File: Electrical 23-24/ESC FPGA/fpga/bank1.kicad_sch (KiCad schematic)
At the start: 1 part, among them U1 XC6SLX4-TQG144

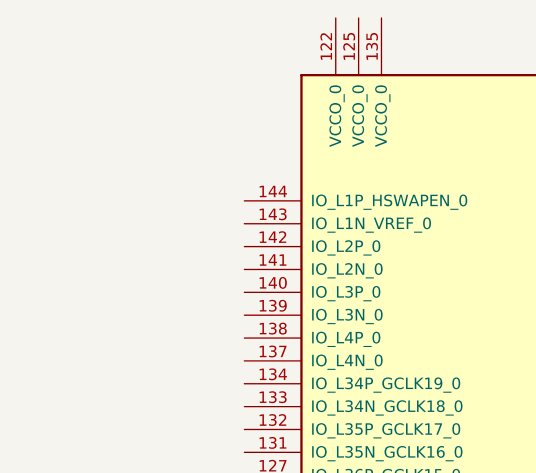
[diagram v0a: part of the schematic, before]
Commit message: Finish programming interface with FPGA
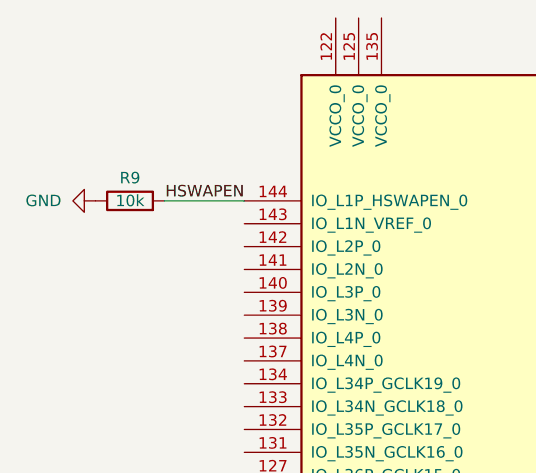
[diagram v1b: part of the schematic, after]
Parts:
- added R9: 10k, symbol Device:R
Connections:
- net HSWAPEN: now reaches U1.144 (IO_L1P_HSWAPEN_0)
- net HSWAPEN: now also R9.2
- new net GND: R9.1
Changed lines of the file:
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@@
 (kicad_sch (version 20230121) (generator eeschema)
   (paper "A4")
+  (wire (pts (xy 40.64 53.34) (xy 49.53 53.34))
+    (stroke (width 0) (type default))
+  )
+  (label "HSWAPEN" (at 49.53 53.34 180) (fields_autoplaced)
+    (effects (font (size 1.27 1.27)) (justify right bottom))
+  )
+  (symbol (lib_id "Device:R") (at 36.83 53.34 90) (unit 1)
+    (in_bom yes) (on_board yes) (dnp no)
+    (property "Reference" "R9" (at 36.83 50.8 90)
+      (effects (font (size 1.27 1.27)))
+    )
+    (property "Value" "10k" (at 36.83 53.34 90)
+      (effects (font (size 1.27 1.27)))
+    )
+    (property "Footprint" "" (at 36.83 55.118 90)
+      (effects (font (size 1.27 1.27)) hide)
+    )
+    (property "Datasheet" "~" (at 36.83 53.34 0)
+      (effects (font (size 1.27 1.27)) hide)
+    )
+    (pin "1")
+    (pin "2")
+    (instances
+      (project "fpga"
+        (path "/5bf59577-a814-4364-8f7a-37815cfb5474/1f83b38b-56ef-4110-879b-13379f9dd920"
+          (reference "R9") (unit 1)
+        )
+      )
+    )
+  )
+  (symbol (lib_id "power:GND") (at 33.02 53.34 270) (unit 1)
+    (in_bom yes) (on_board yes) (dnp no) (fields_autoplaced)
+    (property "Reference" "#PWR06" (at 26.67 53.34 0)
+      (effects (font (size 1.27 1.27)) hide)
+    )
+    (property "Value" "GND" (at 29.21 53.34 90)
+      (effects (font (size 1.27 1.27)) (justify right))
+    )
+    (property "Footprint" "" (at 33.02 53.34 0)
+      (effects (font (size 1.27 1.27)) hide)
+    )
+    (property "Datasheet" "" (at 33.02 53.34 0)
+      (effects (font (size 1.27 1.27)) hide)
+    )
+    (pin "1")
+    (instances
+      (project "fpga"
+        (path "/5bf59577-a814-4364-8f7a-37815cfb5474/a286b274-4434-47ab-983d-e64806fdcbd6"
+          (reference "#PWR06") (unit 1)
+        )
+        (path "/5bf59577-a814-4364-8f7a-37815cfb5474/1f83b38b-56ef-4110-879b-13379f9dd920"
+          (reference "#PWR07") (unit 1)
+        )
+      )
+    )
+  )
   (symbol (lib_id "FPGA_Xilinx_Spartan6:XC6SLX4-TQG144") (at 100.33 76.2 0) (unit 1)
     (in_bom yes) (on_board yes) (dnp no) (fields_autoplaced)

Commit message: idk but something
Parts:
- added C6 (x2): 4u7, symbol Device:C
- added C6 (x4): u47, symbol Device:C
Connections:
- net GND: now also C6.2, C6.2, C6.2, C6.2, C6.2, C6.2
- net VCCO_1: now reaches U1.103 (VCCO_1)
- net VCCO_1: now also U1.76 (VCCO_1), U1.86 (VCCO_1), C6.1, C6.1, C6.1
- net VCCO_0: now reaches U1.122 (VCCO_0)
- net VCCO_0: now also U1.125 (VCCO_0), U1.135 (VCCO_0), C6.1, C6.1, C6.1

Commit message: Add fpga stuff and stencils
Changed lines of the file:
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@@
+    )
+  )
+  (global_label "GND" (shape input) (at 270.51 27.94 90) (fields_autoplaced)
+    (effects (font (size 1.27 1.27)) (justify left))
+    (property "Intersheetrefs" "${INTERSHEET_REFS}" (at 270.51 21.0843 90)
+      (effects (font (size 1.27 1.27)) (justify left) hide)
     )
   )
@@
         )
       )
+    )
+  )
+  (symbol (lib_id "power:GND") (at 270.51 27.94 0) (unit 1)
+    (in_bom yes) (on_board yes) (dnp no) (fields_autoplaced)
+    (property "Reference" "#PWR016" (at 270.51 34.29 0)
+      (effects (font (size 1.27 1.27)) hide)
+    )
+    (property "Value" "GND" (at 270.51 33.02 0)
+      (effects (font (size 1.27 1.27)))
+    )
+    (property "Footprint" "" (at 270.51 27.94 0)
+      (effects (font (size 1.27 1.27)) hide)
+    )
+    (property "Datasheet" "" (at 270.51 27.94 0)
+      (effects (font (size 1.27 1.27)) hide)
+    )
+    (pin "1")
+    (instances
+      (project "fpga"
+        (path "/5bf59577-a814-4364-8f7a-37815cfb5474/3e04db34-3f8a-4742-be82-6fa24c009343"
+          (reference "#PWR016") (unit 1)
+        )
+        (path "/5bf59577-a814-4364-8f7a-37815cfb5474/1f83b38b-56ef-4110-879b-13379f9dd920"
+          (reference "#PWR037") (unit 1)
+        )
+        (path "/5bf59577-a814-4364-8f7a-37815cfb5474/a286b274-4434-47ab-983d-e64806fdcbd6"
+          (reference "#PWR036") (unit 1)
+        )
+      )

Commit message: Working on FPGA board
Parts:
- added J2: LSHM-110-04.0-L-DV-A-N-K-TR, LSHM-110-04.0-L-DV-A-N-K-TR:SAMTEC_LSHM-110-04.0-L-DV-A-N-K-TR, symbol fpga:LSHM-110-04.0-L-DV-A-N-K-TR
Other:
- note added: "where do I put the clock?"
- moved on the sheet: C6, R9, U1A

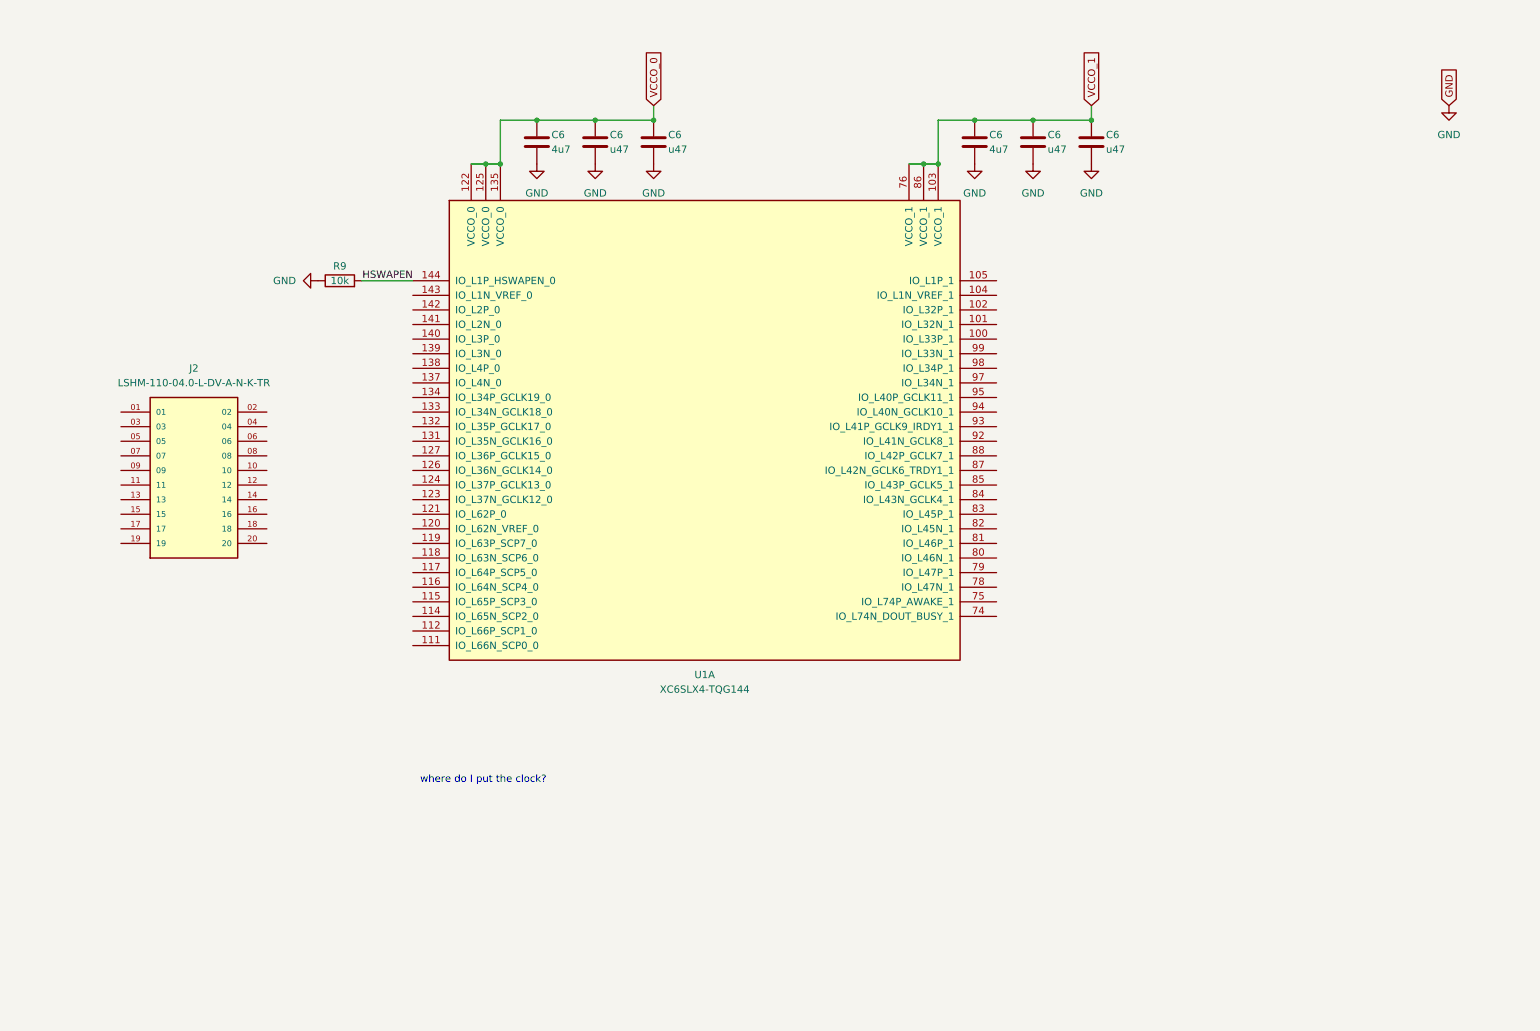
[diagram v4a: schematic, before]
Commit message: Add level shifters
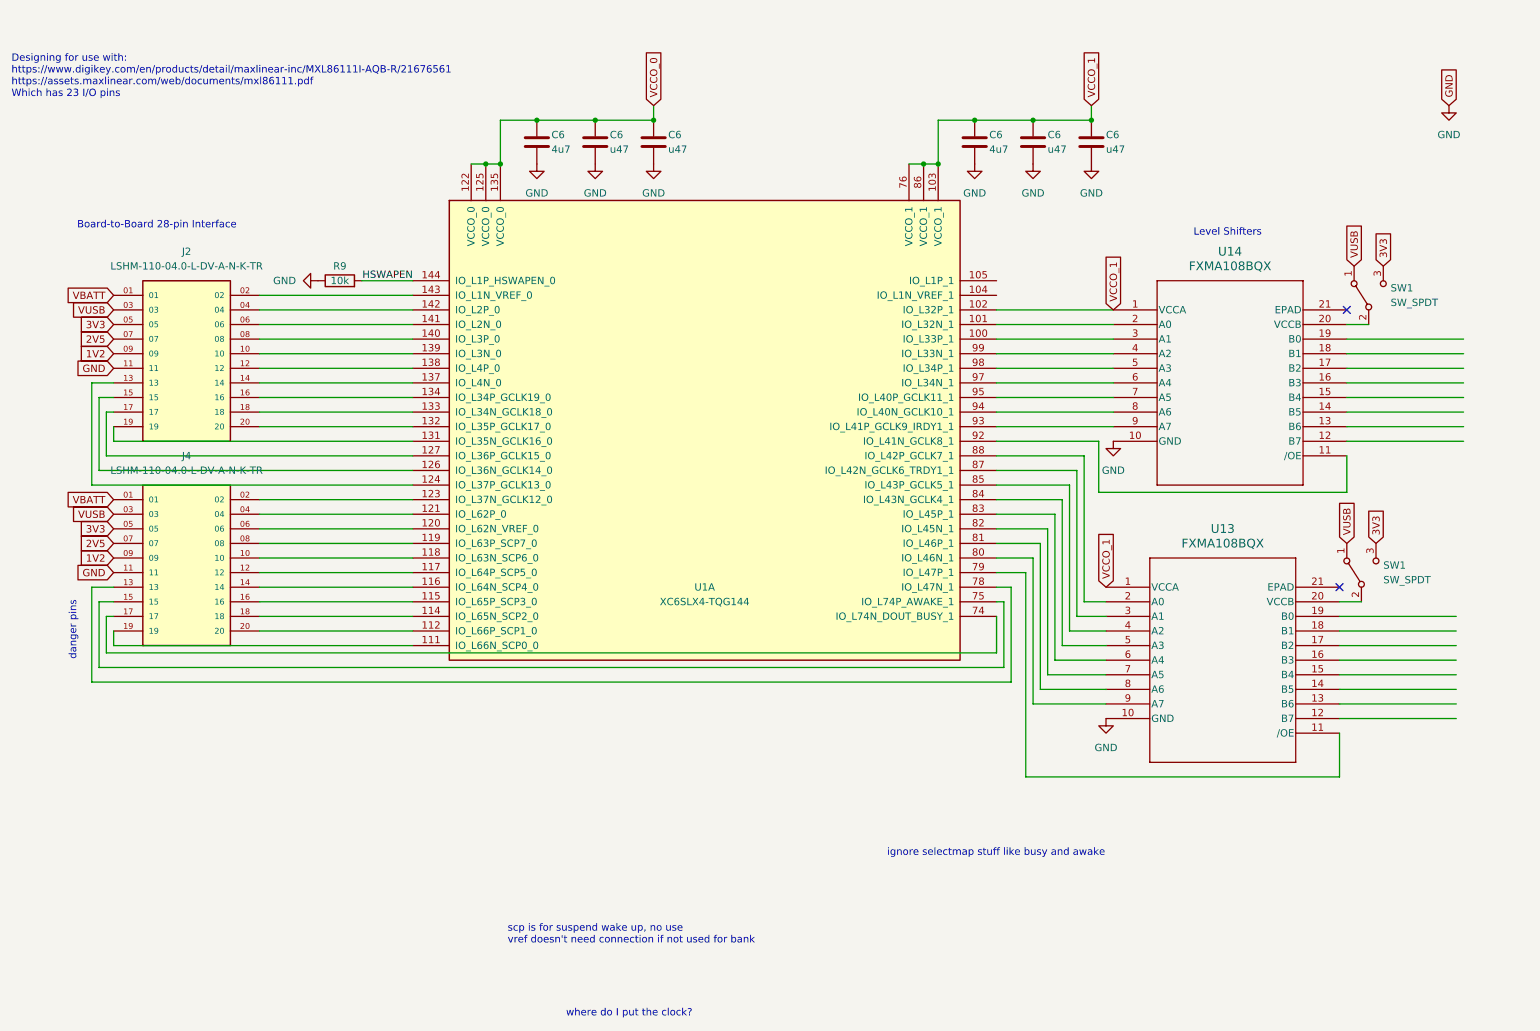
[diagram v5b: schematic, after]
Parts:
- added J4: LSHM-110-04.0-L-DV-A-N-K-TR, LSHM-110-04.0-L-DV-A-N-K-TR:SAMTEC_LSHM-110-04.0-L-DV-A-N-K-TR, symbol fpga:LSHM-110-04.0-L-DV-A-N-K-TR
- added SW1 (x2): SW_SPDT, symbol Switch:SW_SPDT
- added U13, U14: FXMA108BQX, WQFN20_2P5X4P5_ONS, symbol fpga:FXMA108BQX
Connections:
- net GND: now also J2.11, J4.11, U13.10 (GND), U14.10 (GND)
- net VCCO_1: now also U1.102 (IO_L32P_1), U13.1 (VCCA), U14.1 (VCCA)
- net VBATT: now reaches J2.01
- net VBATT: now also J4.01
- net at J2.02: now also U1.143 (IO_L1N_VREF_0)
- net VUSB: now reaches J2.03
- net VUSB: now also J4.03, SW1.1 (A), SW1.1 (A)
- net at J2.04: now also U1.142 (IO_L2P_0)
- net 3V3: now reaches J2.05
- net 3V3: now also J4.05, SW1.3 (C), SW1.3 (C)
- net at J2.06: now also U1.141 (IO_L2N_0)
- net 2V5: now reaches J2.07
- net 2V5: now also J4.07
- net at J2.08: now also U1.140 (IO_L3P_0)
- net 1V2: now reaches J2.09
- net 1V2: now also J4.09
- net at J2.10: now also U1.139 (IO_L3N_0)
- net at J2.12: now also U1.138 (IO_L4P_0)
- net at J2.13: now also U1.124 (IO_L37P_GCLK13_0)
- net at J2.14: now also U1.137 (IO_L4N_0)
- net at J2.15: now also U1.126 (IO_L36N_GCLK14_0)
- net at J2.16: now also U1.134 (IO_L34P_GCLK19_0)
- net at J2.17: now also U1.127 (IO_L36P_GCLK15_0)
- net at J2.18: now also U1.133 (IO_L34N_GCLK18_0)
- net at J2.19: now also U1.131 (IO_L35N_GCLK16_0)
- net at J2.20: now also U1.132 (IO_L35P_GCLK17_0)
- net at U1.100 (IO_L33P_1): now also U14.3 (A1)
- net at U1.101 (IO_L32N_1): now also U14.2 (A0)
- net at U1.111 (IO_L66N_SCP0_0): now also J4.19
- net at U1.112 (IO_L66P_SCP1_0): now also J4.20
- net at U1.114 (IO_L65N_SCP2_0): now also J4.18
- net at U1.115 (IO_L65P_SCP3_0): now also J4.16
- net at U1.116 (IO_L64N_SCP4_0): now also J4.14
- net at U1.117 (IO_L64P_SCP5_0): now also J4.12
- net at U1.118 (IO_L63N_SCP6_0): now also J4.10
- net at U1.119 (IO_L63P_SCP7_0): now also J4.08
- net at U1.120 (IO_L62N_VREF_0): now also J4.06
- net at U1.121 (IO_L62P_0): now also J4.04
- net at U1.123 (IO_L37N_GCLK12_0): now also J4.02
- net at U1.74 (IO_L74N_DOUT_BUSY_1): now also J4.17
- net at U1.75 (IO_L74P_AWAKE_1): now also J4.15
- net at U1.78 (IO_L47N_1): now also J4.13
- net at U1.79 (IO_L47P_1): now also U13.11 (/OE)
- net at U1.80 (IO_L46N_1): now also U13.9 (A7)
- net at U1.81 (IO_L46P_1): now also U13.8 (A6)
- net at U1.82 (IO_L45N_1): now also U13.7 (A5)
- net at U1.83 (IO_L45P_1): now also U13.6 (A4)
- net at U1.84 (IO_L43N_GCLK4_1): now also U13.5 (A3)
- net at U1.85 (IO_L43P_GCLK5_1): now also U13.4 (A2)
- net at U1.87 (IO_L42N_GCLK6_TRDY1_1): now also U13.3 (A1)
- net at U1.88 (IO_L42P_GCLK7_1): now also U13.2 (A0)
- net at U1.92 (IO_L41N_GCLK8_1): now also U14.11 (/OE)
- net at U1.93 (IO_L41P_GCLK9_IRDY1_1): now also U14.9 (A7)
- net at U1.94 (IO_L40N_GCLK10_1): now also U14.8 (A6)
- net at U1.95 (IO_L40P_GCLK11_1): now also U14.7 (A5)
- net at U1.97 (IO_L34N_1): now also U14.6 (A4)
- net at U1.98 (IO_L34P_1): now also U14.5 (A3)
- net at U1.99 (IO_L33N_1): now also U14.4 (A2)
- new net: SW1.2 (B), U13.20 (VCCB)
- new net: SW1.2 (B), U14.20 (VCCB)
- no-connect marks 0 -> 2
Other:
- note added: "Board-to-Board 28-pin Interface"
- note added: "Designing for use with: https://www.digikey.com/en/products/detail/maxlinear-inc/MXL86111I-AQB-R/21676561 https://assets.maxlinear.com/web/documents/mxl86111.pdf Which has 23 I/O pins"
- note added: "Level Shifters"
- note added: "danger pins"
- note added: "ignore selectmap stuff like busy and awake"
- note added: "scp is for suspend wake up, no use vref doesn't need connection if not used for bank"
- moved on the sheet: J2

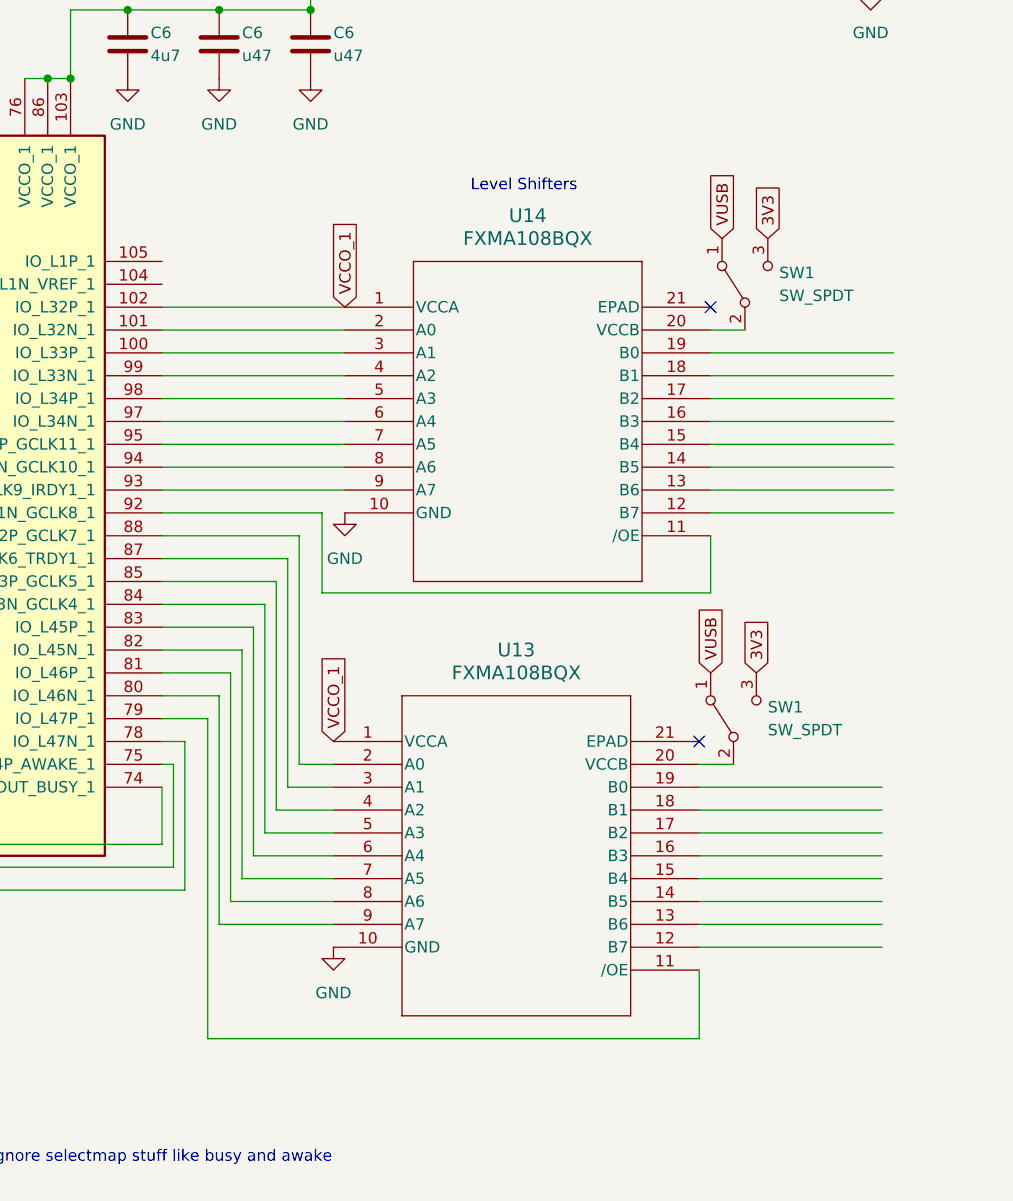
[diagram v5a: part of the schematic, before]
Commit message: Finished FPGA board schematic
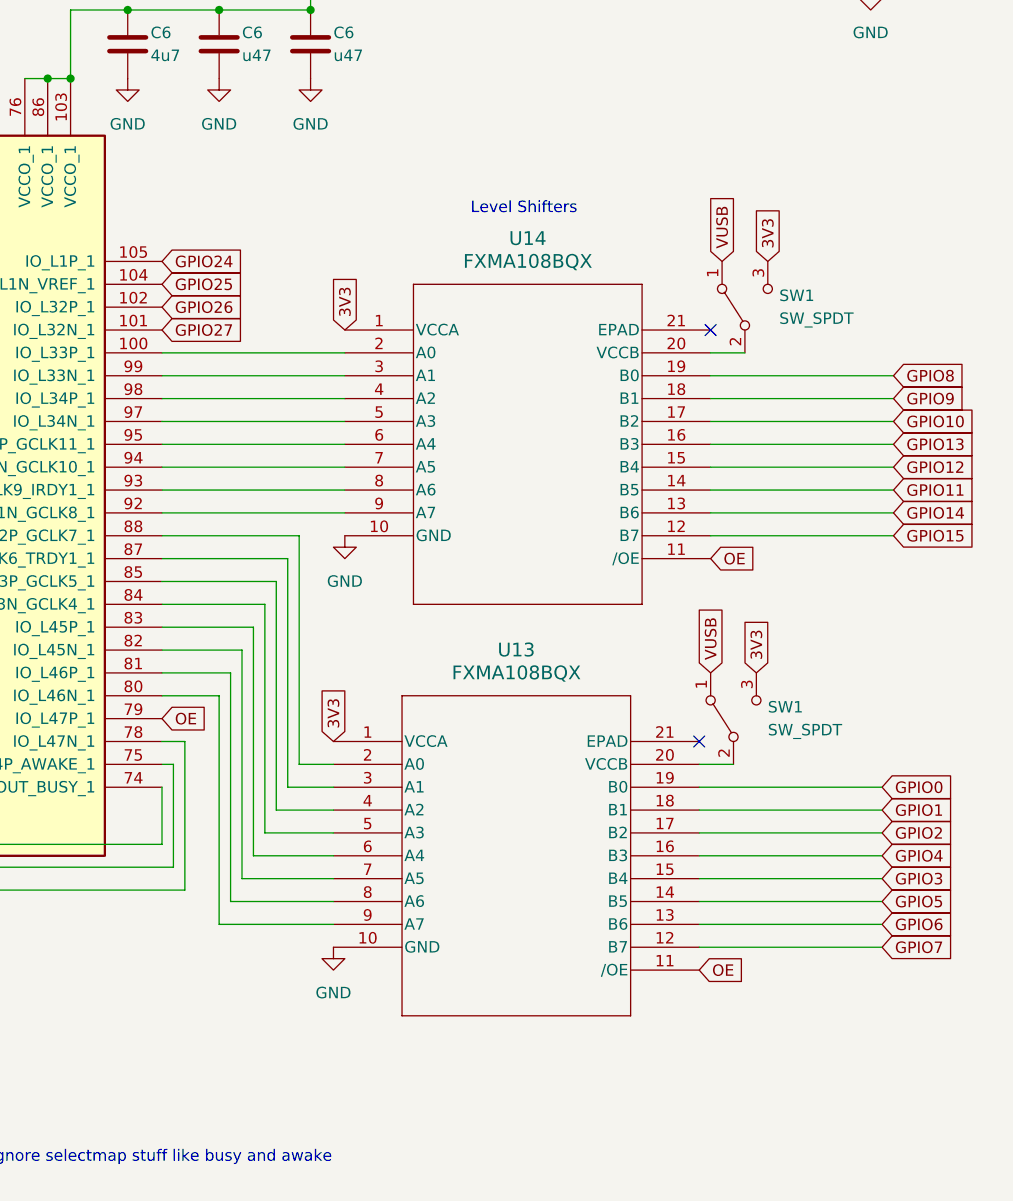
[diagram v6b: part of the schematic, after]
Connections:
- net 3V3: now also U13.1 (VCCA), U14.1 (VCCA)
- net VCCO_1: no longer U1.102 (IO_L32P_1), U13.1 (VCCA), U14.1 (VCCA)
- net OE: now reaches U1.79 (IO_L47P_1), U13.11 (/OE)
- net OE: now also U14.11 (/OE)
- net GPIO7: now reaches U13.12 (B7)
- net GPIO6: now reaches U13.13 (B6)
- net GPIO5: now reaches U13.14 (B5)
- net GPIO3: now reaches U13.15 (B4)
- net GPIO4: now reaches U13.16 (B3)
- net GPIO2: now reaches U13.17 (B2)
- net GPIO1: now reaches U13.18 (B1)
- net GPIO0: now reaches U13.19 (B0)
- net at U1.92 (IO_L41N_GCLK8_1): now also U14.9 (A7); no longer U14.11 (/OE)
- net GPIO15: now reaches U14.12 (B7)
- net GPIO14: now reaches U14.13 (B6)
- net GPIO11: now reaches U14.14 (B5)
- net GPIO12: now reaches U14.15 (B4)
- net GPIO13: now reaches U14.16 (B3)
- net GPIO10: now reaches U14.17 (B2)
- net GPIO9: now reaches U14.18 (B1)
- net GPIO8: now reaches U14.19 (B0)
- net at U14.2 (A0): now also U1.100 (IO_L33P_1); no longer U1.101 (IO_L32N_1)
- net at U14.3 (A1): now also U1.99 (IO_L33N_1); no longer U1.100 (IO_L33P_1)
- net at U14.4 (A2): now also U1.98 (IO_L34P_1); no longer U1.99 (IO_L33N_1)
- net at U14.5 (A3): now also U1.97 (IO_L34N_1); no longer U1.98 (IO_L34P_1)
- net at U14.6 (A4): now also U1.95 (IO_L40P_GCLK11_1); no longer U1.97 (IO_L34N_1)
- net at U14.7 (A5): now also U1.94 (IO_L40N_GCLK10_1); no longer U1.95 (IO_L40P_GCLK11_1)
- net at U14.8 (A6): now also U1.93 (IO_L41P_GCLK9_IRDY1_1); no longer U1.94 (IO_L40N_GCLK10_1)
- net GPIO25: now reaches U1.104 (IO_L1N_VREF_1)
- net GPIO24: now reaches U1.105 (IO_L1P_1)
- new net GPIO26: U1.102 (IO_L32P_1)
- new net GPIO27: U1.101 (IO_L32N_1)
